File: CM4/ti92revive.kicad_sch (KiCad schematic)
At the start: 166 parts

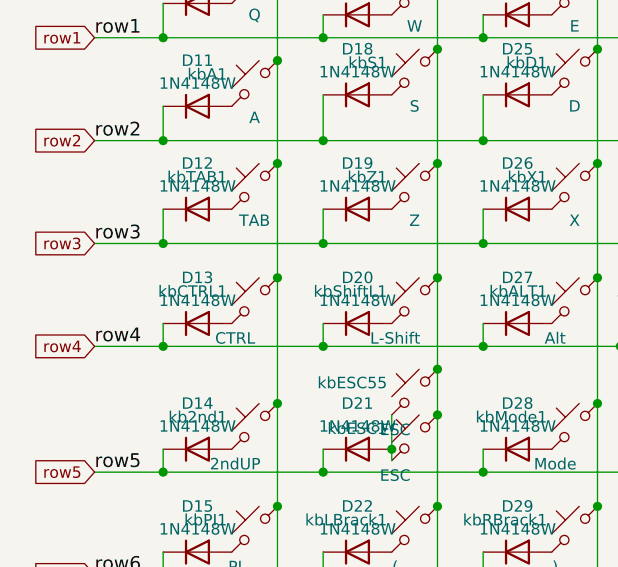
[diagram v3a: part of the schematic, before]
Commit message: Added Power Button Control Circuit
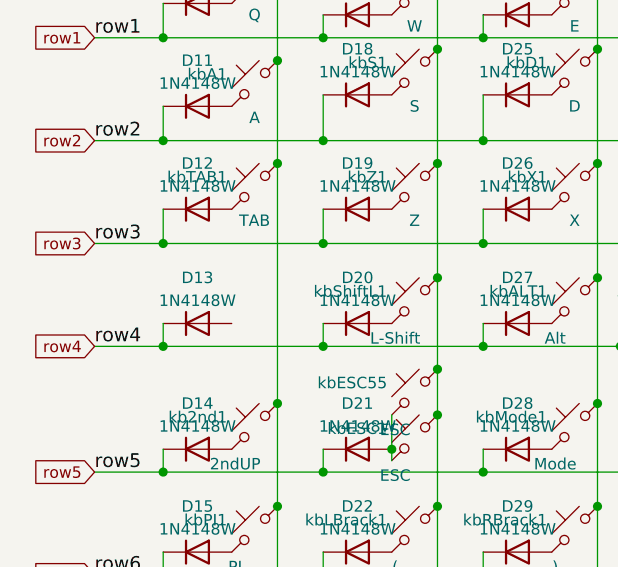
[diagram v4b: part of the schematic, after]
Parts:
- removed kbCTRL1: CTRL, Button_Switch_SMD:SW_SPST_B3SL-1002P, symbol kb5-rescue:SW_Push_45deg-sw_push_45deg-ESP32-S2-WROOM-rescue
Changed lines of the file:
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@@
   (junction (at 49.53 57.15) (diameter 1.016) (color 0 0 0 0))
   (junction (at 49.53 68.58) (diameter 1.016) (color 0 0 0 0))
-  (junction (at 49.53 81.28) (diameter 1.016) (color 0 0 0 0))
   (junction (at 49.53 95.25) (diameter 1.016) (color 0 0 0 0))
   (junction (at 49.53 106.68) (diameter 1.016) (color 0 0 0 0))
@@
     (stroke (width 0) (type solid) (color 0 0 0 0))
   )
-  (wire (pts (xy 49.53 68.58) (xy 49.53 81.28))
-    (stroke (width 0) (type solid) (color 0 0 0 0))
-  )
-  (wire (pts (xy 49.53 81.28) (xy 49.53 95.25))
+  (wire (pts (xy 49.53 68.58) (xy 49.53 95.25))
     (stroke (width 0) (type solid) (color 0 0 0 0))
   )
@@
     (pin "2")
   )
-  (symbol (lib_id "kb5-rescue:SW_Push_45deg-sw_push_45deg-ESP32-S2-WROOM-rescue") (at 46.99 83.82 0) (mirror y) (unit 1)
-    (in_bom yes) (on_board yes)
-    (property "Reference" "kbCTRL1" (id 0) (at 43.942 82.804 0)
-      (effects (font (size 1.27 1.27)) (justify left))
-    )
-    (property "Value" "CTRL" (id 1) (at 44.831 88.011 0))
-    (property "Footprint" "Button_Switch_SMD:SW_SPST_B3SL-1002P" (id 2) (at 46.99 83.82 0)
-      (effects (font (size 1.27 1.27)) hide)
-    )
-    (property "Datasheet" "" (id 3) (at 46.99 83.82 0)
-      (effects (font (size 1.27 1.27)) hide)
-    )
-    (pin "1")
-    (pin "2")
-  )
   (symbol (lib_id "kb5-rescue:SW_Push_45deg-sw_push_45deg-ESP32-S2-WROOM-rescue") (at 46.99 97.79 0) (mirror y) (unit 1)
     (in_bom yes) (on_board yes)
@@
       (reference "kbCOS1") (unit 1) (value "Cos") (footprint "Button_Switch_SMD:SW_SPST_B3SL-1002P")
     )
-    (path "/00000000-0000-0000-0000-00005f46a970"
-      (reference "kbCTRL1") (unit 1) (value "CTRL") (footprint "Button_Switch_SMD:SW_SPST_B3SL-1002P")
-    )
     (path "/00000000-0000-0000-0000-00005f46a9da"
       (reference "kbClear1") (unit 1) (value "Clear") (footprint "Button_Switch_SMD:SW_SPST_B3SL-1002P")
@@
       (reference "#PWR0124") (unit 1) (value "GND") (footprint "")
     )
+    (path "/1ac94e0c-d44c-4ee7-9549-80938fb95f34/95468824-7c1d-443f-a8ac-4660623e14d4"
+      (reference "#PWR0125") (unit 1) (value "GND") (footprint "")
+    )
+    (path "/1ac94e0c-d44c-4ee7-9549-80938fb95f34/01d49955-ce16-4679-84dd-0ff91cf786fb"
+      (reference "#PWR0126") (unit 1) (value "GND") (footprint "")
+    )
+    (path "/1ac94e0c-d44c-4ee7-9549-80938fb95f34/c6da99c8-b4b3-4dbe-be0f-27336a07a512"
+      (reference "#PWR0127") (unit 1) (value "GND") (footprint "")
+    )
     (path "/1ac94e0c-d44c-4ee7-9549-80938fb95f34/80fbd759-c4d6-45da-b3e3-0311235b4d7d"
       (reference "C1") (unit 1) (value "4.7 uF") (footprint "Capacitor_SMD:C_1206_3216Metric")
@@
       (reference "D81") (unit 1) (value "CHG/ERR") (footprint "LED_SMD:LED_2010_5025Metric")
     )
+    (path "/1ac94e0c-d44c-4ee7-9549-80938fb95f34/8b0a5711-f04b-498c-8ef5-a5931db71271"
+      (reference "D82") (unit 1) (value "PWR IND") (footprint "LED_SMD:LED_2010_5025Metric")
+    )
     (path "/1ac94e0c-d44c-4ee7-9549-80938fb95f34/4ff6a8d9-0b28-4bfa-8900-338acb47d18c"
       (reference "J1") (unit 1) (value "USB_B") (footprint "Connector_USB:USB_Micro-B_Amphenol_10103594-0001LF_Horizontal")
@@
       (reference "J3") (unit 1) (value "Conn_01x02") (footprint "Connector_JST:JST_PH_B2B-PH-K_1x02_P2.00mm_Vertical")
     )
+    (path "/1ac94e0c-d44c-4ee7-9549-80938fb95f34/4e784aab-71cc-4c7d-a62b-5b612f67a69c"
+      (reference "JP1") (unit 1) (value "SolderJumper_2_Open") (footprint "Jumper:SolderJumper-2_P1.3mm_Open_RoundedPad1.0x1.5mm")
+    )
     (path "/1ac94e0c-d44c-4ee7-9549-80938fb95f34/418533cd-a032-4d3c-b720-9898a8ff1bef"
       (reference "L1") (unit 1) (value "1uH") (footprint "Inductor_SMD:L_1812_4532Metric")
@@
       (reference "L2") (unit 1) (value "10uH") (footprint "Inductor_SMD:L_1812_4532Metric")
     )
+    (path "/1ac94e0c-d44c-4ee7-9549-80938fb95f34/b3a413b5-1655-4671-94a4-ce23d53b0e41"
+      (reference "Q1") (unit 1) (value "Q_NPN_BCE") (footprint "Package_TO_SOT_SMD:SOT-23")
+    )
     (path "/1ac94e0c-d44c-4ee7-9549-80938fb95f34/d16af4a5-42a2-4b5e-9c3f-f620b161ad34"
       (reference "R1") (unit 1) (value "30.1K") (footprint "Resistor_SMD:R_1206_3216Metric")
@@
       (reference "R11") (unit 1) (value "23.2K") (footprint "Resistor_SMD:R_1206_3216Metric")
     )
+    (path "/1ac94e0c-d44c-4ee7-9549-80938fb95f34/d8c06304-a0b6-484c-ac74-76fe91026dd3"
+      (reference "R12") (unit 1) (value "330") (footprint "Resistor_SMD:R_1206_3216Metric")
+    )
+    (path "/1ac94e0c-d44c-4ee7-9549-80938fb95f34/a75dec26-5524-459e-ad14-b2eb019c0c8b"
+      (reference "R13") (unit 1) (value "330") (footprint "Resistor_SMD:R_1206_3216Metric")
+    )
     (path "/1ac94e0c-d44c-4ee7-9549-80938fb95f34/20efb7b5-d06a-4672-b7fd-f2a22b114571"
       (reference "TH1") (unit 1) (value "10K") (footprint "Connector_PinSocket_2.54mm:PinSocket_1x02_P2.54mm_Vertical")
@@
       (reference "U4") (unit 1) (value "MAX17643") (footprint "trinamic-footprints:TDFN-12_3x3mm_P0.5mm")
     )
+    (path "/1ac94e0c-d44c-4ee7-9549-80938fb95f34/90e9b6d9-586a-40d0-91a9-d7b031629f8a"
+      (reference "U5") (unit 1) (value "ATTINY85-20PU") (footprint "digikey-footprints:DIP-8_W7.62mm")
+    )
+    (path "/1ac94e0c-d44c-4ee7-9549-80938fb95f34/1f2458b3-7fdf-4658-a10e-b0bf6aff31ca"
+      (reference "kbPowerButton1") (unit 1) (value "CTRL") (footprint "Button_Switch_SMD:SW_SPST_B3SL-1002P")
+    )
   )

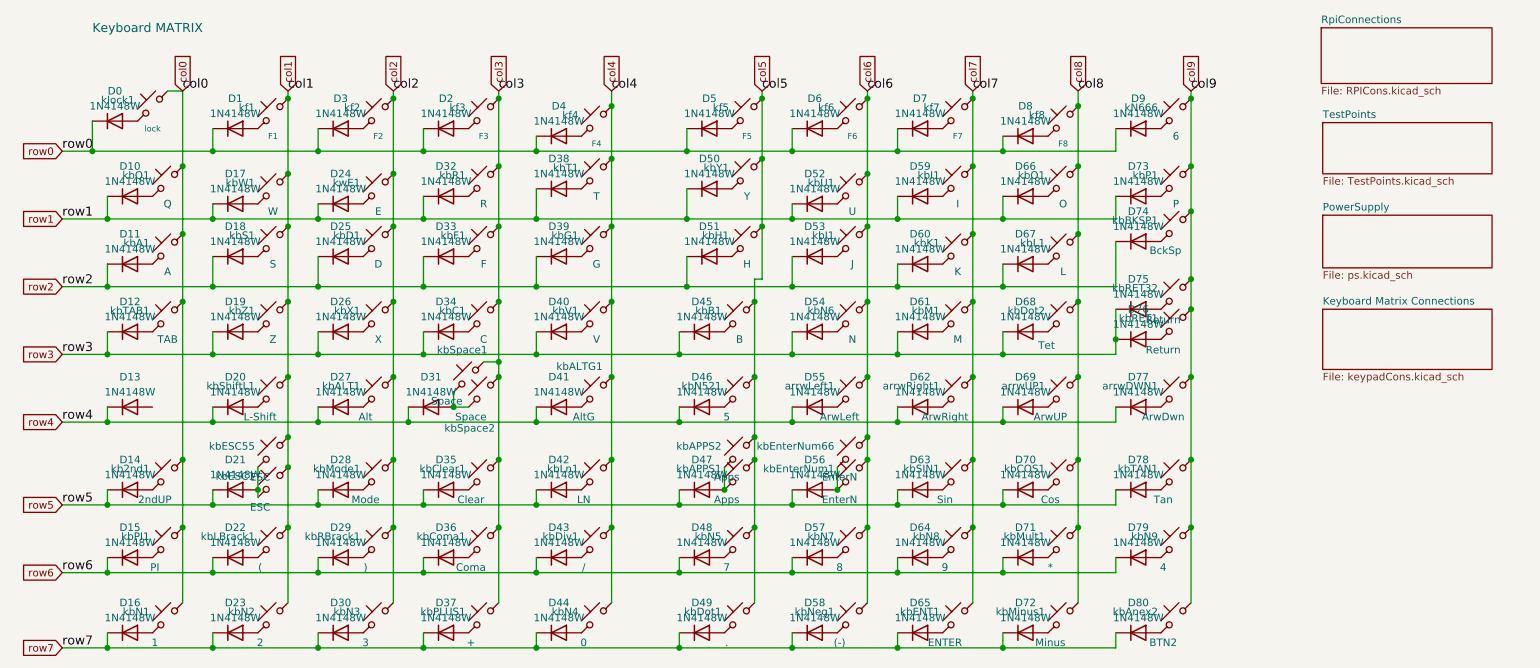
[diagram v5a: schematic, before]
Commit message: Removed Keyboard Matrix Diodes and Added PowerLED and ActivityLED
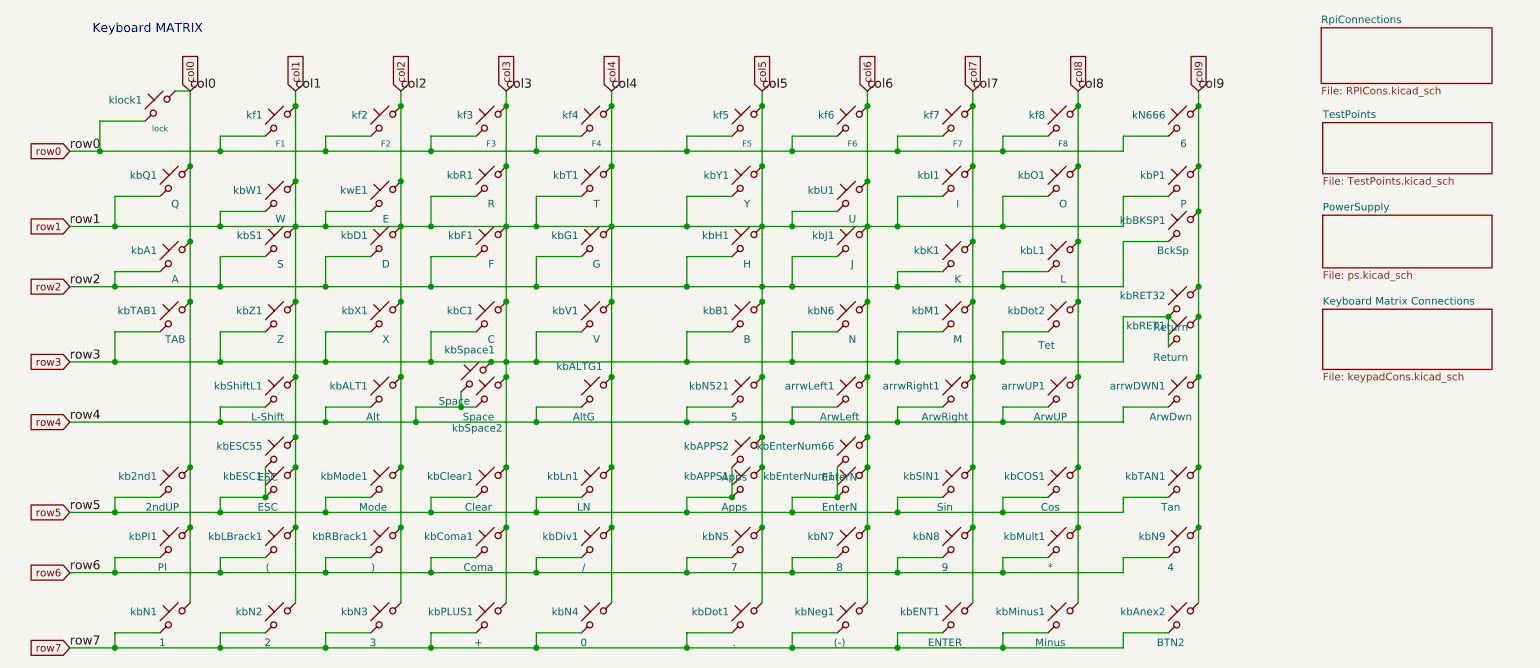
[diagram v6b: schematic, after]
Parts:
- removed D0, D1, D10, D11, D12, D13, D14, D15, D16, D17, D18, D19, D2, D20, D21, D22, D23, D24, D25, D26, D27, D28, D29, D3, D30, D31, D32, D33, D34, D35, D36, D37, D38, D39, D4, D40, D41, D42, D43, D44, D45, D46, D47, D48, D49, D5, D50, D51, D52, D53, D54, D55, D56, D57, D58, D59, D6, D60, D61, D62, D63, D64, D65, D66, D67, D68, D69, D7, D70, D71, D72, D73, D74, D75, D76, D77, D78, D79, D8, D80, D9: 1N4148W, Diode_SMD:D_SOD-123, symbol Diode:1N4148W
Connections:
- net col2 is gone; now on net col1: kbALT1.1, kbD1.1, kbMode1.1, kbN3.1, kbRBrack1.1, kbX1.1, kf2.1, kwE1.1
- net col3 is gone; now on net col1: kbC1.1, kbClear1.1, kbComa1.1, kbF1.1, kbPLUS1.1, kbR1.1, kbSpace1.1, kbSpace2.1, kf3.1
- net col4 is gone; now on net col1: kbALTG1.1, kbDiv1.1, kbG1.1, kbLn1.1, kbN4.1, kbT1.1, kbV1.1, kf4.1
- net col5 is gone; now on net col1: kbAPPS1.1, kbAPPS2.1, kbB1.1, kbDot1.1, kbH1.1, kbN5.1, kbN521.1, kbY1.1, kf5.1
- net col6 is gone; now on net col1: arrwLeft1.1, kbEnterNum1.1, kbEnterNum66.1, kbJ1.1, kbN6.1, kbN7.1, kbNeg1.1, kbU1.1, kf6.1
- net col1: now also kbA1.2, kbB1.2, kbBKSP1.2, kbC1.2, kbD1.2, kbDot2.2, kbF1.2, kbG1.2, kbH1.2, kbI1.2, kbJ1.2, kbK1.2, kbL1.2, kbM1.2, kbN6.2, kbO1.2, kbP1.2, kbQ1.2, kbR1.2, kbRET1.2, kbRET32.2, kbS1.2, kbT1.2, kbTAB1.2, kbU1.2, kbV1.2, kbW1.2, kbX1.2, kbY1.2, kbZ1.2, kwE1.2
- net row0: now also kN666.2, kf1.2, kf2.2, kf3.2, kf4.2, kf5.2, kf6.2, kf7.2, kf8.2, klock1.2
- net row4: now also arrwDWN1.2, arrwLeft1.2, arrwRight1.2, arrwUP1.2, kbALT1.2, kbALTG1.2, kbN521.2, kbShiftL1.2, kbSpace1.2, kbSpace2.2
- net row5: now also kb2nd1.2, kbAPPS1.2, kbAPPS2.2, kbCOS1.2, kbClear1.2, kbESC1.2, kbESC55.2, kbEnterNum1.2, kbEnterNum66.2, kbLn1.2, kbMode1.2, kbSIN1.2, kbTAN1.2
- net row6: now also kbComa1.2, kbDiv1.2, kbLBrack1.2, kbMult1.2, kbN5.2, kbN7.2, kbN8.2, kbN9.2, kbPI1.2, kbRBrack1.2
- net row7: now also kbAnex2.2, kbDot1.2, kbENT1.2, kbMinus1.2, kbN1.2, kbN2.2, kbN3.2, kbN4.2, kbNeg1.2, kbPLUS1.2
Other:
- moved on the sheet: arrwDWN1, kN666, kb2nd1, kbA1, kbALT1, kbAPPS1, kbAPPS2, kbAnex2, kbB1, kbBKSP1, kbC1, kbCOS1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

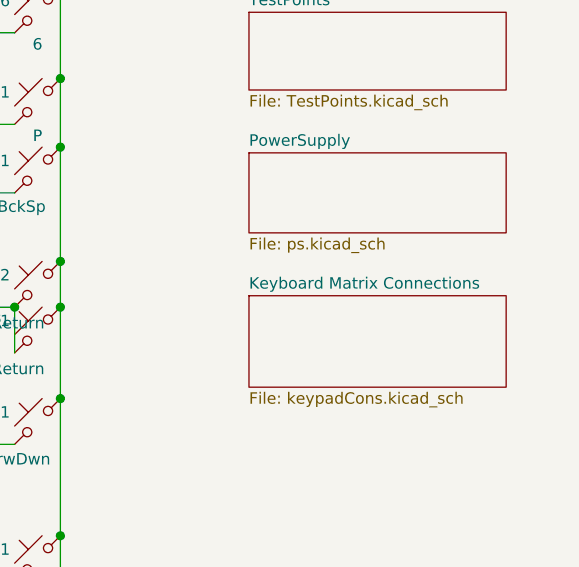
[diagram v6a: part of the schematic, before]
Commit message: Added high current 3.3v supply
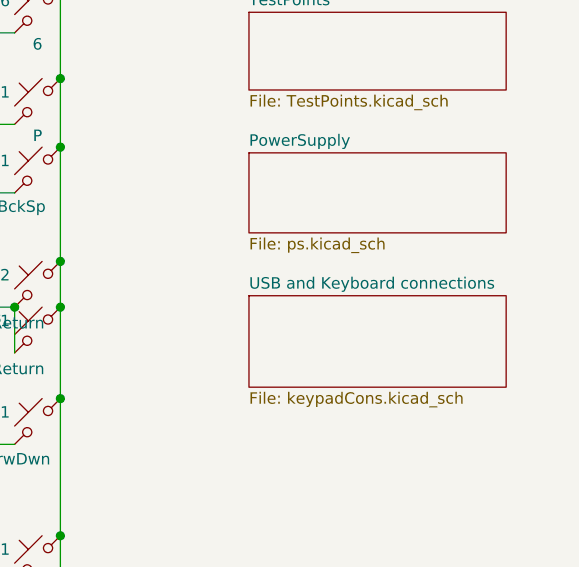
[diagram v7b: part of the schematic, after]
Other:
- sheet Keyboard Matrix Connections renamed USB and Keyboard connections
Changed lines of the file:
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@@
     (pin "2")
-  )
-  (sheet (at 241.935 69.85) (size 28.575 10.16)
-    (stroke (width 0.0006) (type solid) (color 0 0 0 0))
-    (fill (color 0 0 0 0.0000))
-    (property "Sheet name" "Keyboard Matrix Connections" (id 0) (at 241.935 69.2143 0)
-      (effects (font (size 1.27 1.27)) (justify left bottom))
-    )
-    (property "Sheet file" "keypadCons.kicad_sch" (id 1) (at 241.935 80.5187 0)
-      (effects (font (size 1.27 1.27)) (justify left top))
-    )
   )
   (sheet (at 241.935 53.975) (size 28.575 8.89)
@@
     )
     (property "Sheet file" "TestPoints.kicad_sch" (id 1) (at 241.935 47.4987 0)
+      (effects (font (size 1.27 1.27)) (justify left top))
+    )
+  )
+  (sheet (at 241.935 69.85) (size 28.575 10.16)
+    (stroke (width 0.0006) (type solid) (color 0 0 0 0))
+    (fill (color 0 0 0 0.0000))
+    (property "Sheet name" "USB and Keyboard connections" (id 0) (at 241.935 69.2143 0)
+      (effects (font (size 1.27 1.27)) (justify left bottom))
+    )
+    (property "Sheet file" "keypadCons.kicad_sch" (id 1) (at 241.935 80.5187 0)
       (effects (font (size 1.27 1.27)) (justify left top))
     )
@@
     )
     (path "/5d98706f-d271-406b-9d01-9a0abd3931f8/efddf7d7-25b1-4157-9149-ddf2be1495df"
-      (reference "TP12") (unit 1) (value "USB_OTG_ID_TP") (footprint "")
+      (reference "TP12") (unit 1) (value "USB_OTG_ID_TP") (footprint "TestPoint:TestPoint_Pad_D1.0mm")
     )
     (path "/5d98706f-d271-406b-9d01-9a0abd3931f8/e33133e0-fc58-4981-bd2e-26b87cd36954"
@@
       (reference "#PWR0129") (unit 1) (value "GND") (footprint "")
     )
+    (path "/1ac94e0c-d44c-4ee7-9549-80938fb95f34/264017f1-90e9-41ac-bc61-3c4cd423311a"
+      (reference "#PWR0131") (unit 1) (value "GND") (footprint "")
+    )
+    (path "/1ac94e0c-d44c-4ee7-9549-80938fb95f34/47e264c8-28ec-4add-b778-4b54ecfcc8a9"
+      (reference "#PWR0132") (unit 1) (value "GND") (footprint "")
+    )
+    (path "/1ac94e0c-d44c-4ee7-9549-80938fb95f34/ab14938e-a875-4e8c-bb9d-f2db6468077f"
+      (reference "#PWR0133") (unit 1) (value "GND") (footprint "")
+    )
     (path "/1ac94e0c-d44c-4ee7-9549-80938fb95f34/80fbd759-c4d6-45da-b3e3-0311235b4d7d"
       (reference "C1") (unit 1) (value "4.7 uF") (footprint "Capacitor_SMD:C_1206_3216Metric")
@@
       (reference "C11") (unit 1) (value "22uF") (footprint "Capacitor_SMD:C_1206_3216Metric")
     )
+    (path "/1ac94e0c-d44c-4ee7-9549-80938fb95f34/7837710e-0644-450f-93a5-ae91e8f84463"
+      (reference "C12") (unit 1) (value "10 uF") (footprint "Capacitor_SMD:C_1206_3216Metric")
+    )
+    (path "/1ac94e0c-d44c-4ee7-9549-80938fb95f34/f6ec5553-9e4a-483f-bed3-747f1afc7776"
+      (reference "C13") (unit 1) (value "10 uF") (footprint "Capacitor_SMD:C_1206_3216Metric")
+    )
     (path "/1ac94e0c-d44c-4ee7-9549-80938fb95f34/e5902921-eea8-4549-81f4-54f1666f3a72"
       (reference "D81") (unit 1) (value "CHG/ERR") (footprint "LED_SMD:LED_2010_5025Metric")
@@
       (reference "TP11") (unit 1) (value "TS") (footprint "TestPoint:TestPoint_Pad_1.0x1.0mm")
     )
+    (path "/1ac94e0c-d44c-4ee7-9549-80938fb95f34/cfd44934-7283-4e57-be21-7e0082b17f87"
+      (reference "U2") (unit 1) (value "NCP114ASN330T1G") (footprint "Package_TO_SOT_SMD:TSOT-23-5_HandSoldering")
+    )
     (path "/1ac94e0c-d44c-4ee7-9549-80938fb95f34/42717736-8383-4ae5-a746-4cc3d5884ee8"
